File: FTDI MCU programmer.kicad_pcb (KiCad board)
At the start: 2 copper layers, 38.2 x 19 mm, 19 parts, among them J1 VCC MCU Select, J2 MCU IO, J3 USB_B_Micro, J5 BreadBoard IO, J6 BreadBoard IO, U1 FT232RQ

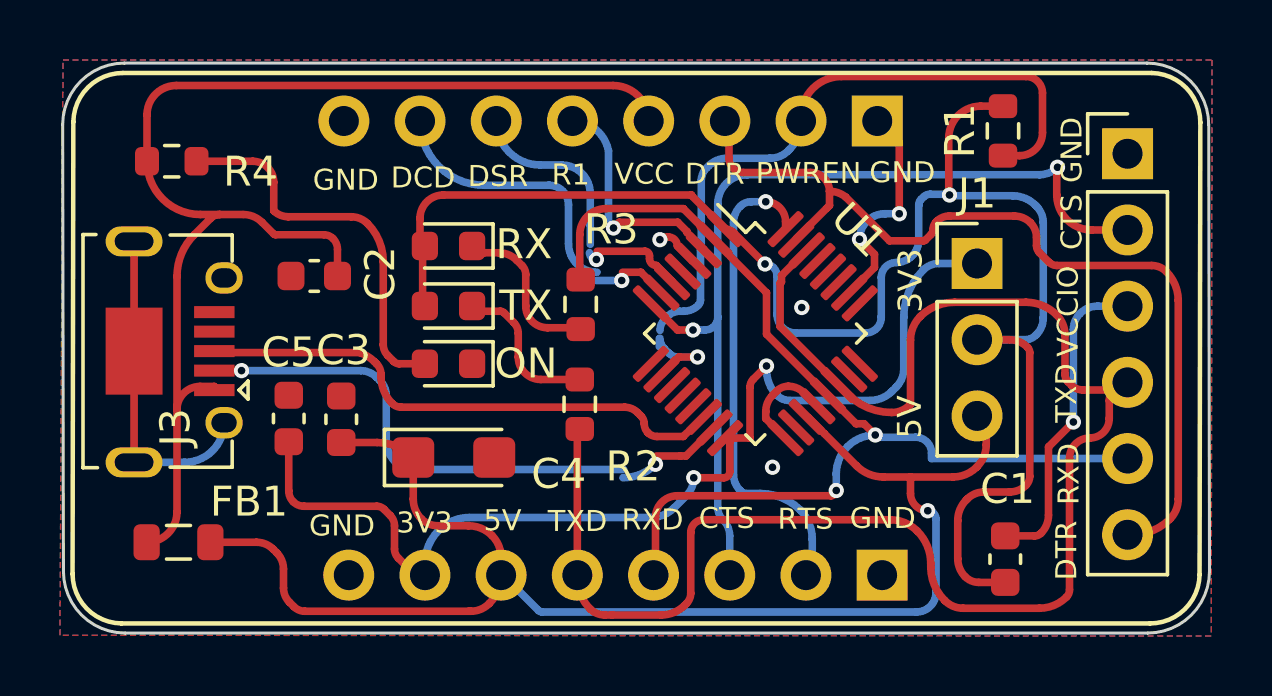
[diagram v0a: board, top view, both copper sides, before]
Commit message: fixed a trace error
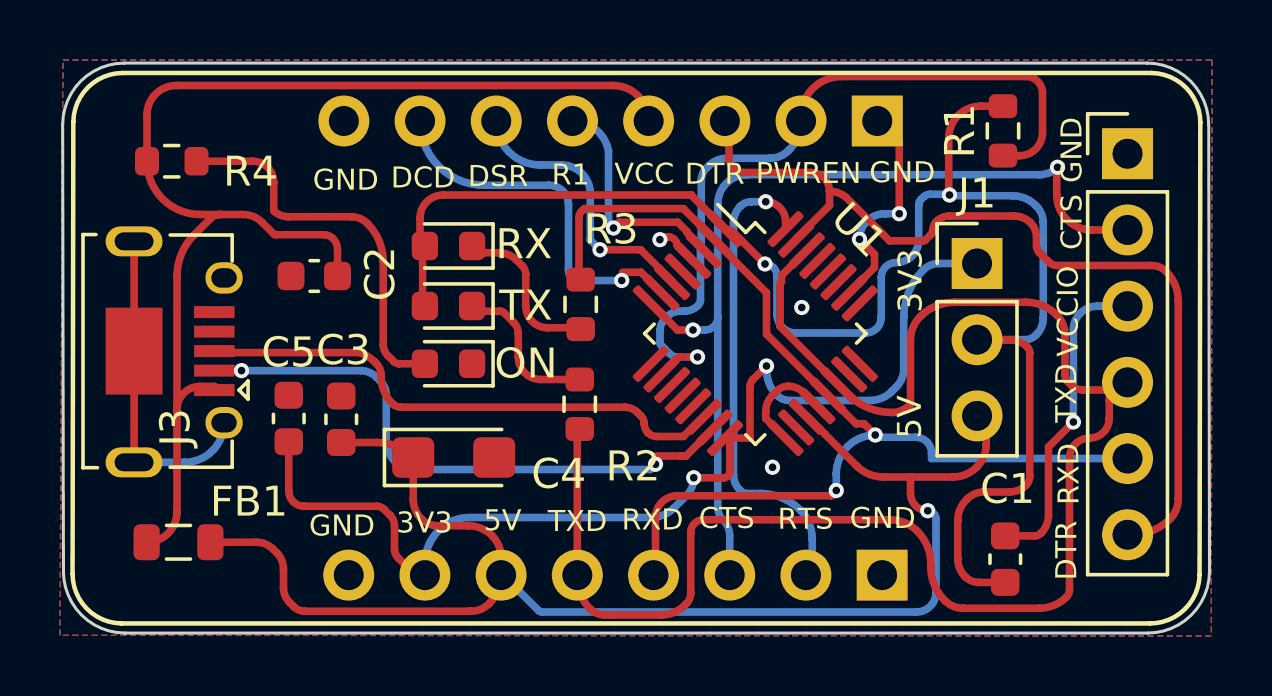
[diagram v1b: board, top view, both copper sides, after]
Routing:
- net /DCD: track 11.6 -> 12.2 mm
